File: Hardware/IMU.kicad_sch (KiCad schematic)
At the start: 0 parts

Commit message: Checkpoint
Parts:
- added U4: ICM-20948, Sensor_Motion:InvenSense_QFN-24_3x3mm_P0.4mm, symbol Sensor_Motion:ICM-20948
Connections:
- new net: U4.18 (GND), U4.20 (GND)
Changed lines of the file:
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@@
 (kicad_sch (version 20230121) (generator eeschema)
   (paper "A4")
+  (hierarchical_label "VDD" (shape passive) (at 152.4 101.6 0) (fields_autoplaced)
+    (effects (font (size 1.27 1.27)) (justify left))
+  )
+  (symbol (lib_id "Sensor_Motion:ICM-20948") (at 139.7 66.04 0) (unit 1)
+    (in_bom yes) (on_board yes) (dnp no) (fields_autoplaced)
+    (property "Reference" "U4" (at 141.6559 83.82 0)
+      (effects (font (size 1.27 1.27)) (justify left))
+    )
+    (property "Value" "ICM-20948" (at 141.6559 86.36 0)
+      (effects (font (size 1.27 1.27)) (justify left))
+    )
+    (property "Footprint" "Sensor_Motion:InvenSense_QFN-24_3x3mm_P0.4mm" (at 139.7 91.44 0)
+      (effects (font (size 1.27 1.27)) hide)
+    )
+    (property "Datasheet" "http://www.invensense.com/wp-content/uploads/2016/06/DS-000189-ICM-20948-v1.3.pdf" (at 139.7 69.85 0)
+      (effects (font (size 1.27 1.27)) hide)
+    )
+    (pin "1")
+    (pin "10")
+    (pin "11")
+    (pin "12")
+    (pin "13")
+    (pin "14")
+    (pin "15")
+    (pin "16")
+    (pin "17")
+    (pin "18")
+    (pin "19")
+    (pin "2")
+    (pin "20")
+    (pin "21")
+    (pin "22")
+    (pin "23")
+    (pin "24")
+    (pin "3")
+    (pin "4")
+    (pin "5")
+    (pin "6")
+    (pin "7")
+    (pin "8")
+    (pin "9")
+    (instances
+      (project "Avionus_Flight_Controller"
+        (path "/ddc7e940-0588-4587-8902-8ced9e615ace/7fdd9ac2-b3bc-40e6-909c-cb884a3f310d"
+          (reference "U4") (unit 1)
+        )
+      )
+    )
+  )
 )

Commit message: Checkpoint
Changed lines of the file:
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@@
 (kicad_sch (version 20230121) (generator eeschema)
   (paper "A4")
+  (hierarchical_label "NCS" (shape input) (at 76.2 58.42 0) (fields_autoplaced)
+    (effects (font (size 1.27 1.27)) (justify left))
+  )
+  (hierarchical_label "VIO" (shape passive) (at 152.4 104.14 0) (fields_autoplaced)
+    (effects (font (size 1.27 1.27)) (justify left))
+  )
+  (hierarchical_label "SCLK" (shape input) (at 76.2 55.88 0) (fields_autoplaced)
+    (effects (font (size 1.27 1.27)) (justify left))
+  )
+  (hierarchical_label "SDI" (shape input) (at 76.2 50.8 0) (fields_autoplaced)
+    (effects (font (size 1.27 1.27)) (justify left))
+  )
+  (hierarchical_label "INT1" (shape output) (at 76.2 63.5 0) (fields_autoplaced)
+    (effects (font (size 1.27 1.27)) (justify left))
+  )
   (hierarchical_label "VDD" (shape passive) (at 152.4 101.6 0) (fields_autoplaced)
     (effects (font (size 1.27 1.27)) (justify left))
   )
+  (hierarchical_label "SDO" (shape output) (at 76.2 53.34 0) (fields_autoplaced)
+    (effects (font (size 1.27 1.27)) (justify left))
+  )

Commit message: Checkpoint
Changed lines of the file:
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@@
     (effects (font (size 1.27 1.27)) (justify left))
   )
-  (hierarchical_label "VIO" (shape passive) (at 152.4 104.14 0) (fields_autoplaced)
+  (hierarchical_label "VDD_1V8" (shape passive) (at 152.4 104.14 0) (fields_autoplaced)
     (effects (font (size 1.27 1.27)) (justify left))
   )
@@
     (effects (font (size 1.27 1.27)) (justify left))
   )
-  (hierarchical_label "VDD" (shape passive) (at 152.4 101.6 0) (fields_autoplaced)
+  (hierarchical_label "VDD_3V3" (shape passive) (at 152.4 101.6 0) (fields_autoplaced)
     (effects (font (size 1.27 1.27)) (justify left))
   )

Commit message: Checkpoint
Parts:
- added C23: 100nF, symbol Device:C_Small
- added Q1 (x5): RE1C002UN, Package_TO_SOT_SMD:SOT-416, symbol Device:Q_NMOS_GSD
- added R14 (x5), R15 (x5): 2.2K, symbol Device:R_Small
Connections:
- net INT1: now also Q1.3 (D), R15.1
- net NCS: now also Q1.3 (D), R15.1
- net SCLK: now also Q1.3 (D), R15.1
- net SDI: now also Q1.3 (D), R15.1
- net SDO: now also Q1.3 (D), R15.1
- net VDD_1V8: now also U4.13 (VDD), U4.8 (VDDIO), Q1.1 (G), Q1.1 (G), Q1.1 (G), Q1.1 (G), Q1.1 (G), R14.2, R14.2, R14.2, R14.2, R14.2
- net VDD_3V3: now also R15.2, R15.2, R15.2, R15.2, R15.2
- net at U4.10 (REGOUT): now also C23.1
- net INT1_VIO: now reaches U4.12 (INT1)
- net INT1_VIO: now also Q1.2 (S), R14.1
- net GND: now reaches U4.18 (GND), U4.20 (GND)
- net GND: now also C23.2
- net NCS_VIO: now reaches U4.22 (~{CS})
- net NCS_VIO: now also Q1.2 (S), R14.1
- net SCLK_VIO: now reaches U4.23 (SCL/SCLK)
- net SCLK_VIO: now also Q1.2 (S), R14.1
- net SDI_VIO: now reaches U4.24 (SDA/SDI)
- net SDI_VIO: now also Q1.2 (S), R14.1
- net SDO_VIO: now reaches U4.9 (SDO/AD0)
- net SDO_VIO: now also Q1.2 (S), R14.1
- no-connect marks 0 -> 3
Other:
- moved on the sheet: U4

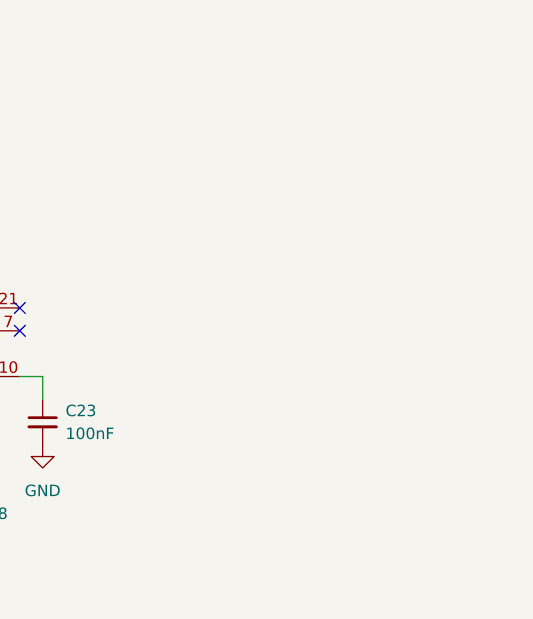
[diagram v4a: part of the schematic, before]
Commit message: Add IMU supply capacitors
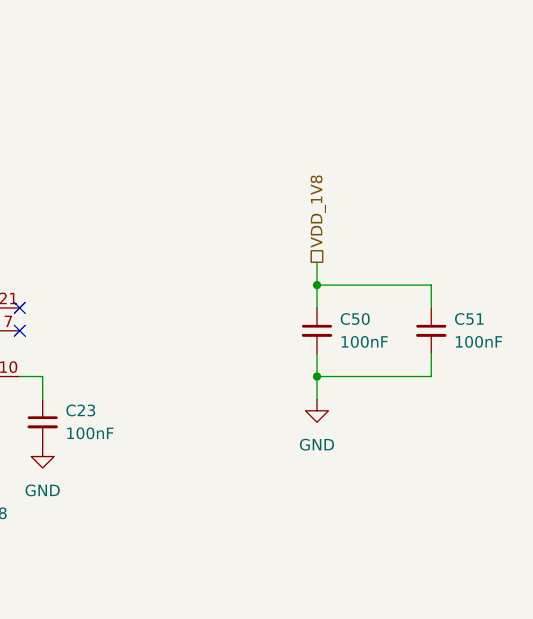
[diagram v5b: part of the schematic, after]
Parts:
- added C50, C51: 100nF, symbol Device:C_Small
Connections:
- net GND: now also C50.2, C51.2
- net VDD_1V8: now also C50.1, C51.1
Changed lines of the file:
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@@
   (junction (at 50.8 109.22) (diameter 0) (color 0 0 0 0)
   )
+  (junction (at 185.42 86.36) (diameter 0) (color 0 0 0 0)
+  )
   (junction (at 50.8 58.42) (diameter 0) (color 0 0 0 0)
   )
@@
   )
   (junction (at 35.56 109.22) (diameter 0) (color 0 0 0 0)
+  )
+  (junction (at 185.42 96.52) (diameter 0) (color 0 0 0 0)
   )
   (no_connect (at 127 96.52))
@@
     (stroke (width 0) (type default))
   )
+  (wire (pts (xy 185.42 96.52) (xy 198.12 96.52))
+    (stroke (width 0) (type default))
+  )
   (wire (pts (xy 50.8 83.82) (xy 48.26 83.82))
     (stroke (width 0) (type default))
@@
     (stroke (width 0) (type default))
   )
+  (wire (pts (xy 185.42 96.52) (xy 185.42 99.06))
+    (stroke (width 0) (type default))
+  )
+  (wire (pts (xy 185.42 86.36) (xy 185.42 83.82))
+    (stroke (width 0) (type default))
+  )
   (wire (pts (xy 50.8 96.52) (xy 50.8 99.06))
     (stroke (width 0) (type default))
@@
     (stroke (width 0) (type default))
   )
+  (wire (pts (xy 198.12 88.9) (xy 198.12 86.36))
+    (stroke (width 0) (type default))
+  )
+  (wire (pts (xy 185.42 88.9) (xy 185.42 86.36))
+    (stroke (width 0) (type default))
+  )
   (wire (pts (xy 33.02 121.92) (xy 50.8 121.92))
     (stroke (width 0) (type default))
@@
     (stroke (width 0) (type default))
   )
+  (wire (pts (xy 185.42 93.98) (xy 185.42 96.52))
+    (stroke (width 0) (type default))
+  )
   (wire (pts (xy 35.56 104.14) (xy 35.56 109.22))
     (stroke (width 0) (type default))
@@
     (stroke (width 0) (type default))
   )
+  (wire (pts (xy 198.12 96.52) (xy 198.12 93.98))
+    (stroke (width 0) (type default))
+  )
   (wire (pts (xy 50.8 53.34) (xy 50.8 58.42))
     (stroke (width 0) (type default))
@@
   )
   (wire (pts (xy 35.56 109.22) (xy 38.1 109.22))
+    (stroke (width 0) (type default))
+  )
+  (wire (pts (xy 185.42 86.36) (xy 198.12 86.36))
     (stroke (width 0) (type default))
   )
@@
     (effects (font (size 1.27 1.27)) (justify left))
   )
+  (hierarchical_label "VDD_1V8" (shape passive) (at 185.42 83.82 90) (fields_autoplaced)
+    (effects (font (size 1.27 1.27)) (justify left))
+  )
   (hierarchical_label "SDI" (shape input) (at 53.34 58.42 0) (fields_autoplaced)
     (effects (font (size 1.27 1.27)) (justify left))
@@
     )
   )
+  (symbol (lib_id "Device:C_Small") (at 185.42 91.44 0) (unit 1)
+    (in_bom yes) (on_board yes) (dnp no)
+    (property "Reference" "C50" (at 187.96 90.1763 0)
+      (effects (font (size 1.27 1.27)) (justify left))
+    )
+    (property "Value" "100nF" (at 187.96 92.7163 0)
+      (effects (font (size 1.27 1.27)) (justify left))
+    )
+    (property "Footprint" "" (at 185.42 91.44 0)
+      (effects (font (size 1.27 1.27)) hide)
+    )
+    (property "Datasheet" "~" (at 185.42 91.44 0)
+      (effects (font (size 1.27 1.27)) hide)
+    )
+    (pin "1")
+    (pin "2")
+    (instances
+      (project "Avionus_Flight_Controller"
+        (path "/ddc7e940-0588-4587-8902-8ced9e615ace/7fdd9ac2-b3bc-40e6-909c-cb884a3f310d"
+          (reference "C50") (unit 1)
+        )
+      )
+    )
+  )
   (symbol (lib_id "Device:Q_NMOS_GSD") (at 43.18 81.28 270) (unit 1)
     (in_bom yes) (on_board yes) (dnp no) (fields_autoplaced)
@@
         (path "/ddc7e940-0588-4587-8902-8ced9e615ace/7fdd9ac2-b3bc-40e6-909c-cb884a3f310d"
           (reference "Q16") (unit 1)
+        )
+      )
+    )
+  )
+  (symbol (lib_id "Device:C_Small") (at 198.12 91.44 0) (unit 1)
+    (in_bom yes) (on_board yes) (dnp no) (fields_autoplaced)
+    (property "Reference" "C51" (at 200.66 90.1763 0)
+      (effects (font (size 1.27 1.27)) (justify left))
+    )
+    (property "Value" "100nF" (at 200.66 92.7163 0)
+      (effects (font (size 1.27 1.27)) (justify left))
+    )
+    (property "Footprint" "" (at 198.12 91.44 0)
+      (effects (font (size 1.27 1.27)) hide)
+    )
+    (property "Datasheet" "~" (at 198.12 91.44 0)
+      (effects (font (size 1.27 1.27)) hide)
+    )
+    (pin "1")
+    (pin "2")
+    (instances
+      (project "Avionus_Flight_Controller"
+        (path "/ddc7e940-0588-4587-8902-8ced9e615ace/7fdd9ac2-b3bc-40e6-909c-cb884a3f310d"
+          (reference "C51") (unit 1)
         )
       )
@@
         )
       )
+    )
+  )
+  (symbol (lib_id "power:GND") (at 185.42 99.06 0) (unit 1)
+    (in_bom yes) (on_board yes) (dnp no) (fields_autoplaced)
+    (property "Reference" "#PWR056" (at 185.42 105.41 0)
+      (effects (font (size 1.27 1.27)) hide)
+    )
+    (property "Value" "GND" (at 185.42 104.14 0)
+      (effects (font (size 1.27 1.27)))
+    )
+    (property "Footprint" "" (at 185.42 99.06 0)
+      (effects (font (size 1.27 1.27)) hide)
+    )
+    (property "Datasheet" "" (at 185.42 99.06 0)
+      (effects (font (size 1.27 1.27)) hide)
+    )
+    (pin "1")
+    (instances
+      (project "Avionus_Flight_Controller"
+        (path "/ddc7e940-0588-4587-8902-8ced9e615ace/7fdd9ac2-b3bc-40e6-909c-cb884a3f310d"
+          (reference "#PWR056") (unit 1)
+        )
+      )

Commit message: Checkpoint
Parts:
- renumbered C23 to C1501, C50 to C1502, C51 to C1503, Q1 to Q?, R14 to R?, R15 to R?, U4 to U1501

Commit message: Checkpoint
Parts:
- C1501, C1502, C1503: footprint (none) -> Capacitor_SMD:C_0603_1608Metric
- R? (x10): footprint (none) -> Resistor_SMD:R_0805_2012Metric
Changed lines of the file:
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@@
       (effects (font (size 1.27 1.27)) (justify left))
     )
-    (property "Footprint" "" (at 185.42 91.44 0)
+    (property "Footprint" "Capacitor_SMD:C_0603_1608Metric" (at 185.42 91.44 0)
       (effects (font (size 1.27 1.27)) hide)
     )
@@
       (effects (font (size 1.27 1.27)) (justify left))
     )
-    (property "Footprint" "" (at 198.12 91.44 0)
+    (property "Footprint" "Capacitor_SMD:C_0603_1608Metric" (at 198.12 91.44 0)
       (effects (font (size 1.27 1.27)) hide)
     )
@@
       (effects (font (size 1.27 1.27)) (justify right))
     )
-    (property "Footprint" "" (at 35.56 127 0)
+    (property "Footprint" "Resistor_SMD:R_0805_2012Metric" (at 35.56 127 0)
       (effects (font (size 1.27 1.27)) hide)
     )
@@
       (effects (font (size 1.27 1.27)) (justify right))
     )
-    (property "Footprint" "" (at 35.56 25.4 0)
+    (property "Footprint" "Resistor_SMD:R_0805_2012Metric" (at 35.56 25.4 0)
       (effects (font (size 1.27 1.27)) hide)
     )
@@
       (effects (font (size 1.27 1.27)) (justify right))
     )
-    (property "Footprint" "" (at 35.56 76.2 0)
+    (property "Footprint" "Resistor_SMD:R_0805_2012Metric" (at 35.56 76.2 0)
       (effects (font (size 1.27 1.27)) hide)
     )
@@
       (effects (font (size 1.27 1.27)) (justify right))
     )
-    (property "Footprint" "" (at 35.56 50.8 0)
+    (property "Footprint" "Resistor_SMD:R_0805_2012Metric" (at 35.56 50.8 0)
       (effects (font (size 1.27 1.27)) hide)
     )
@@
       (effects (font (size 1.27 1.27)) (justify left))
     )
-    (property "Footprint" "" (at 154.94 101.6 0)
+    (property "Footprint" "Capacitor_SMD:C_0603_1608Metric" (at 154.94 101.6 0)
       (effects (font (size 1.27 1.27)) hide)
     )
@@
       (effects (font (size 1.27 1.27)) (justify right))
     )
-    (property "Footprint" "" (at 50.8 127 0)
+    (property "Footprint" "Resistor_SMD:R_0805_2012Metric" (at 50.8 127 0)
       (effects (font (size 1.27 1.27)) hide)
     )
@@
       (effects (font (size 1.27 1.27)) (justify right))
     )
-    (property "Footprint" "" (at 50.8 76.2 0)
+    (property "Footprint" "Resistor_SMD:R_0805_2012Metric" (at 50.8 76.2 0)
       (effects (font (size 1.27 1.27)) hide)
     )
@@
       (effects (font (size 1.27 1.27)) (justify right))
     )
-    (property "Footprint" "" (at 35.56 101.6 0)
+    (property "Footprint" "Resistor_SMD:R_0805_2012Metric" (at 35.56 101.6 0)
       (effects (font (size 1.27 1.27)) hide)
     )
@@
       (effects (font (size 1.27 1.27)) (justify right))
     )
-    (property "Footprint" "" (at 50.8 101.6 0)
+    (property "Footprint" "Resistor_SMD:R_0805_2012Metric" (at 50.8 101.6 0)
       (effects (font (size 1.27 1.27)) hide)
     )
@@
       (effects (font (size 1.27 1.27)) (justify right))
     )
-    (property "Footprint" "" (at 50.8 25.4 0)
+    (property "Footprint" "Resistor_SMD:R_0805_2012Metric" (at 50.8 25.4 0)
       (effects (font (size 1.27 1.27)) hide)
     )
@@
       (effects (font (size 1.27 1.27)) (justify right))
     )
-    (property "Footprint" "" (at 50.8 50.8 0)
-      (effects (font (size 1.27 1.27)) hide)
-    )
+    (property "Footprint" "Resistor_SMD:R_0805_2012Metric" (at 50.8 50.8 0)
+      (effects (font (size 1.27 1.27)) hide)
+    )

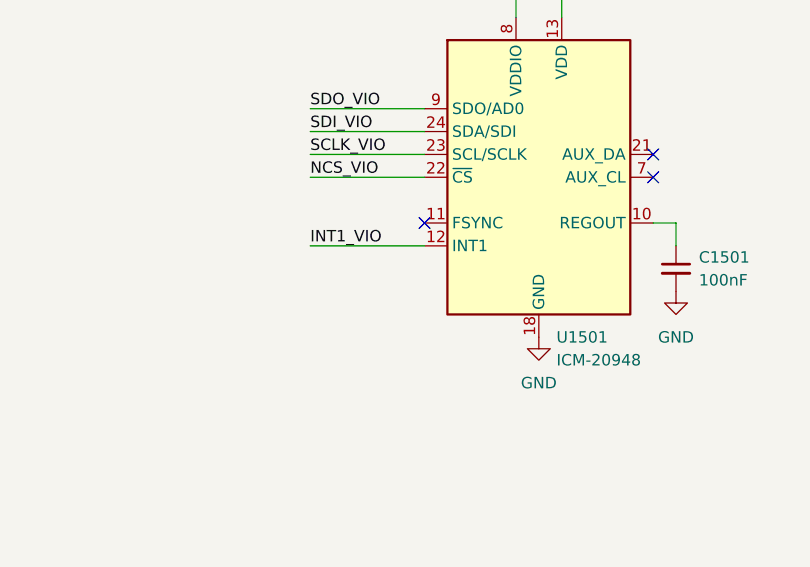
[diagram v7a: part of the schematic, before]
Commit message: IMU FSYNC to GND
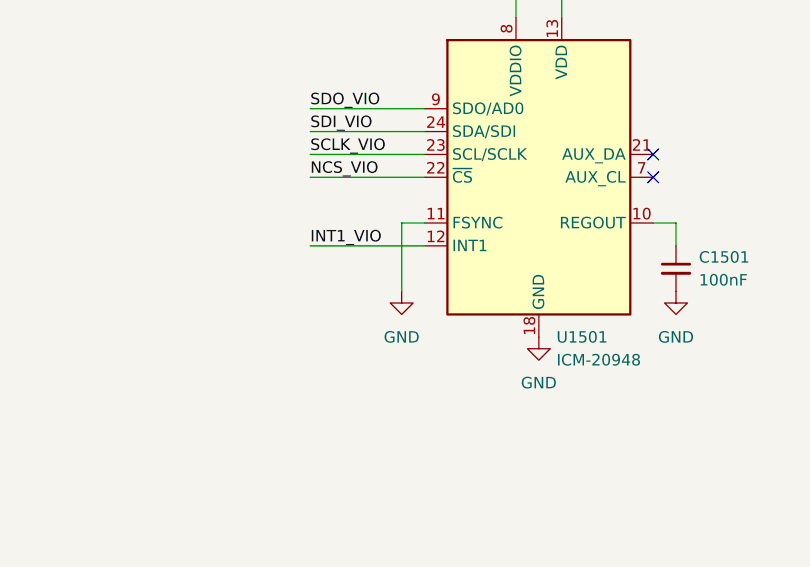
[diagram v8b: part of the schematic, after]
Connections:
- net GND: now also U1501.11 (FSYNC)
- no-connect marks 3 -> 2
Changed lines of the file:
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@@
   (junction (at 185.42 96.52) (diameter 0) (color 0 0 0 0)
   )
-  (no_connect (at 127 96.52))
   (no_connect (at 152.4 88.9))
   (no_connect (at 152.4 91.44))
@@
     (stroke (width 0) (type default))
   )
+  (wire (pts (xy 124.46 96.52) (xy 124.46 104.14))
+    (stroke (width 0) (type default))
+  )
   (wire (pts (xy 33.02 73.66) (xy 35.56 73.66))
     (stroke (width 0) (type default))
@@
   )
   (wire (pts (xy 50.8 58.42) (xy 48.26 58.42))
+    (stroke (width 0) (type default))
+  )
+  (wire (pts (xy 127 96.52) (xy 124.46 96.52))
     (stroke (width 0) (type default))
   )
@@
         )
       )
+    )
+  )
+  (symbol (lib_id "power:GND") (at 124.46 104.14 0) (unit 1)
+    (in_bom yes) (on_board yes) (dnp no) (fields_autoplaced)
+    (property "Reference" "#PWR01504" (at 124.46 110.49 0)
+      (effects (font (size 1.27 1.27)) hide)
+    )
+    (property "Value" "GND" (at 124.46 109.22 0)
+      (effects (font (size 1.27 1.27)))
+    )
+    (property "Footprint" "" (at 124.46 104.14 0)
+      (effects (font (size 1.27 1.27)) hide)
+    )
+    (property "Datasheet" "" (at 124.46 104.14 0)
+      (effects (font (size 1.27 1.27)) hide)
+    )
+    (pin "1")
+    (instances
+      (project "Avionus_Flight_Controller"
+        (path "/ddc7e940-0588-4587-8902-8ced9e615ace/7fdd9ac2-b3bc-40e6-909c-cb884a3f310d"
+          (reference "#PWR01504") (unit 1)
+        )
+      )
